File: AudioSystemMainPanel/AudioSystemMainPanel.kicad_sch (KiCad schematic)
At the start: 29 parts, among them J1 AudioPlug3, U1 DEVKIT_V1_ESP32-WROOM-32, U2 PCM5102A, U3 OPA2134, U4 OPA2134

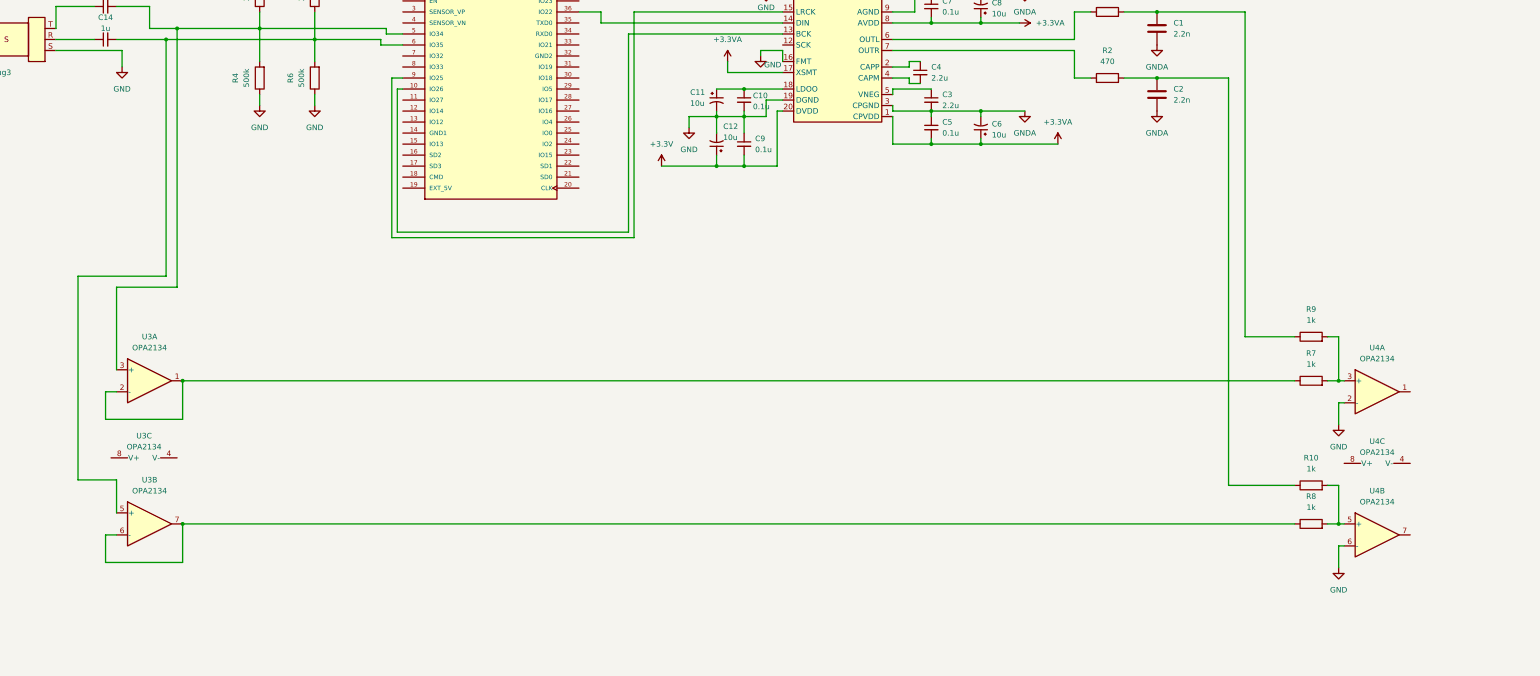
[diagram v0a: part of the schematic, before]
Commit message: added filter/eq panel, small fixes for main panel
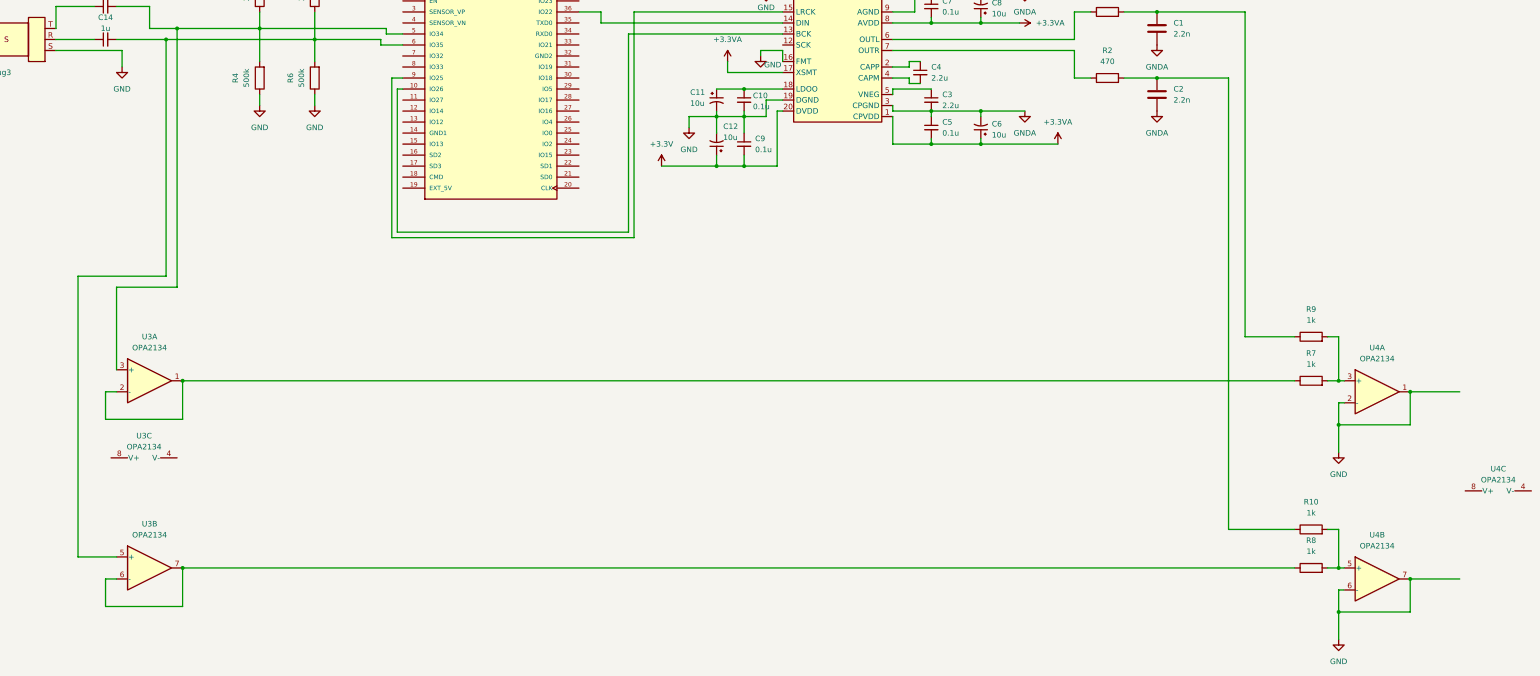
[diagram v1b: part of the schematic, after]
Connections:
- net GND: now also U4.1, U4.7
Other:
- moved on the sheet: R10, R8, U3B, U4B, U4C

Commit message: created noise cancellation panel, added a custom symbol library to project
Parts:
- removed U1: DEVKIT_V1_ESP32-WROOM-32, DEVKIT_V1_ESP32-WROOM-32:MODULE_DEVKIT_V1_ESP32-WROOM-32, symbol DEVKIT_V1_ESP32-WROOM-32:DEVKIT_V1_ESP32-WROOM-32
- added U1: DEVKIT_V1_ESP32-WROOM-32, DEVKIT_V1_ESP32-WROOM-32:MODULE_DEVKIT_V1_ESP32-WROOM-32, symbol AudioSystemSymbolLibrary:DEVKIT_V1_ESP32-WROOM-32
- U3, U4: footprint (none) -> AudioSystemFootprintLibrary:OPA2134UA
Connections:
- net at C14.2, R5.1, R6.2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: now also U1.6 (IO35)
- net at C13.2, R3.1, R4.2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: now also U1.5 (IO34)
- net at U2.13 (BCK): now also U1.10 (IO26)
- net at U2.14 (DIN): now also U1.36 (IO22)
- net at U2.15 (LRCK): now also U1.9 (IO25)
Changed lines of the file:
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@@
 			)
 		)
-		(property "Footprint" ""
+		(property "Footprint" "AudioSystemFootprintLibrary:OPA2134UA"
 			(at 66.04 171.45 0)
 			(effects
@@
 			)
 		)
-		(property "Footprint" ""
+		(property "Footprint" "AudioSystemFootprintLibrary:OPA2134UA"
 			(at 349.25 130.81 0)
 			(effects
@@
 			)
 		)
-		(property "Footprint" ""
+		(property "Footprint" "AudioSystemFootprintLibrary:OPA2134UA"
 			(at 377.19 151.13 0)
 			(effects
@@
 			)
 		)
-		(property "Footprint" ""
+		(property "Footprint" "AudioSystemFootprintLibrary:OPA2134UA"
 			(at 349.25 173.99 0)
 			(effects
@@
 	)
 	(symbol
-		(lib_id "Device:C")
-		(at 298.45 46.99 0)
-		(unit 1)
-		(exclude_from_sim no)
-		(in_bom yes)
-		(on_board yes)
-		(dnp no)
-		(fields_autoplaced yes)
-		(property "Reference" "C1"
-			(at 302.26 45.7199 0)
-			(effects
-				(font
-					(size 1.27 1.27)
-				)
-				(justify left)
-			)
-		)
-		(property "Value" "2.2n"
-			(at 302.26 48.2599 0)
-			(effects
-				(font
-					(size 1.27 1.27)
-				)
-				(justify left)
-			)
-		)
-		(property "Footprint" ""
-			(at 299.4152 50.8 0)
-			(effects
-				(font
-					(size 1.27 1.27)
-				)
-				(hide yes)
-			)
-		)
-		(property "Datasheet" "~"
-			(at 298.45 46.99 0)
-			(effects
-				(font
-					(size 1.27 1.27)
-				)
-				(hide yes)
-			)
-		)
-		(property "Description" "Unpolarized capacitor"
-			(at 298.45 46.99 0)
-			(effects
-				(font
-					(size 1.27 1.27)
-				)
-				(hide yes)
-			)
-		)
-		(pin "1"
-		)
-		(pin "2"
-		)
-		(instances
-			(project ""
-				(path "/ff53e594-6401-4e7d-9332-9d87eb1f5f5d"
-					(reference "C1")
-					(unit 1)
-				)
-			)
-		)
-	)
-	(symbol
-		(lib_id "power:GND")
-		(at 104.14 64.77 0)
-		(unit 1)
-		(exclude_from_sim no)
-		(in_bom yes)
-		(on_board yes)
-		(dnp no)
-		(fields_autoplaced yes)
-		(property "Reference" "#PWR014"
-			(at 104.14 71.12 0)
-			(effects
-				(font
-					(size 1.27 1.27)
-				)
-				(hide yes)
-			)
-		)
-		(property "Value" "GND"
-			(at 104.14 69.85 0)
-			(effects
-				(font
-					(size 1.27 1.27)
-				)
-			)
-		)
-		(property "Footprint" ""
-			(at 104.14 64.77 0)
-			(effects
-				(font
-					(size 1.27 1.27)
-				)
-				(hide yes)
-			)
-		)
-		(property "Datasheet" ""
-			(at 104.14 64.77 0)
-			(effects
-				(font
-					(size 1.27 1.27)
-				)
-				(hide yes)
-			)
-		)
-		(property "Description" "Power symbol creates a global label with name \"GND\" , ground"
-			(at 104.14 64.77 0)
-			(effects
-				(font
-					(size 1.27 1.27)
-				)
-				(hide yes)
-			)
-		)
-		(pin "1"
-		)
-		(instances
-			(project ""
-				(path "/ff53e594-6401-4e7d-9332-9d87eb1f5f5d"
-					(reference "#PWR014")
-					(unit 1)
-				)
-			)
-		)
-	)
-	(symbol
-		(lib_id "DEVKIT_V1_ESP32-WROOM-32:DEVKIT_V1_ESP32-WROOM-32")
+		(lib_id "AudioSystemSymbolLibrary:DEVKIT_V1_ESP32-WROOM-32")
 		(at 144.78 60.96 0)
 		(unit 1)
@@
 			)
 		)
-		(pin "1"
+		(pin "32"
 		)
-		(pin "18"
+		(pin "30"
 		)
-		(pin "2"
+		(pin "6"
 		)
-		(pin "32"
+		(pin "4"
 		)
-		(pin "9"
+		(pin "17"
 		)
-		(pin "27"
+		(pin "12"
 		)
-		(pin "30"
+		(pin "13"
+		)
+		(pin "8"
+		)
+		(pin "33"
+		)
+		(pin "22"
 		)
 		(pin "29"
 		)
-		(pin "15"
+		(pin "34"
 		)
-		(pin "28"
+		(pin "35"
 		)
-		(pin "4"
+		(pin "38"
 		)
-		(pin "24"
+		(pin "9"
 		)
-		(pin "6"
+		(pin "18"
 		)
-		(pin "23"
+		(pin "20"
 		)
-		(pin "12"
+		(pin "25"
 		)
 		(pin "14"
 		)
-		(pin "20"
+		(pin "26"
+		)
+		(pin "37"
 		)
 		(pin "21"
 		)
+		(pin "27"
+		)
+		(pin "28"
+		)
+		(pin "16"
+		)
 		(pin "10"
 		)
-		(pin "3"
+		(pin "2"
 		)
-		(pin "36"
+		(pin "31"
 		)
 		(pin "7"
 		)
-		(pin "22"
+		(pin "15"
+		)
+		(pin "23"
+		)
+		(pin "1"
+		)
+		(pin "3"
+		)
+		(pin "24"
+		)
+		(pin "5"
 		)
 		(pin "11"
@@
 		(pin "19"
 		)
-		(pin "25"
+		(pin "36"
 		)
-		(pin "8"
+		(instances
+			(project ""
+				(path "/ff53e594-6401-4e7d-9332-9d87eb1f5f5d"
+					(reference "U1")
+					(unit 1)
+				)
+			)
 		)
-		(pin "13"
+	)
+	(symbol
+		(lib_id "Device:C")
+		(at 298.45 46.99 0)
+		(unit 1)
+		(exclude_from_sim no)
+		(in_bom yes)
+		(on_board yes)
+		(dnp no)
+		(fields_autoplaced yes)
+		(property "Reference" "C1"
+			(at 302.26 45.7199 0)
+			(effects
+				(font
+					(size 1.27 1.27)
+				)
+				(justify left)
+			)
 		)
-		(pin "16"
+		(property "Value" "2.2n"
+			(at 302.26 48.2599 0)
+			(effects
+				(font
+					(size 1.27 1.27)
+				)
+				(justify left)
+			)
 		)
-		(pin "33"
+		(property "Footprint" ""
+			(at 299.4152 50.8 0)
+			(effects
+				(font
+					(size 1.27 1.27)
+				)
+				(hide yes)
+			)
 		)
-		(pin "37"
+		(property "Datasheet" "~"
+			(at 298.45 46.99 0)
+			(effects
+				(font
+					(size 1.27 1.27)
+				)
+				(hide yes)
+			)
 		)
-		(pin "5"
+		(property "Description" "Unpolarized capacitor"
+			(at 298.45 46.99 0)
+			(effects
+				(font
+					(size 1.27 1.27)
+				)
+				(hide yes)
+			)
 		)
-		(pin "34"
+		(pin "1"
 		)
-		(pin "38"
+		(pin "2"
 		)
-		(pin "26"
+		(instances
+			(project ""
+				(path "/ff53e594-6401-4e7d-9332-9d87eb1f5f5d"
+					(reference "C1")
+					(unit 1)
+				)
+			)
 		)
-		(pin "31"
+	)
+	(symbol
+		(lib_id "power:GND")
+		(at 104.14 64.77 0)
+		(unit 1)
+		(exclude_from_sim no)
+		(in_bom yes)
+		(on_board yes)
+		(dnp no)
+		(fields_autoplaced yes)
+		(property "Reference" "#PWR014"
+			(at 104.14 71.12 0)
+			(effects
+				(font
+					(size 1.27 1.27)
+				)
+				(hide yes)
+			)
 		)
-		(pin "17"
+		(property "Value" "GND"
+			(at 104.14 69.85 0)
+			(effects
+				(font
+					(size 1.27 1.27)
+				)
+			)
 		)
-		(pin "35"
+		(property "Footprint" ""
+			(at 104.14 64.77 0)
+			(effects
+				(font
+					(size 1.27 1.27)
+				)
+				(hide yes)
+			)
+		)
+		(property "Datasheet" ""
+			(at 104.14 64.77 0)
+			(effects
+				(font
+					(size 1.27 1.27)
+				)
+				(hide yes)
+			)
+		)
+		(property "Description" "Power symbol creates a global label with name \"GND\" , ground"
+			(at 104.14 64.77 0)
+			(effects
+				(font
+					(size 1.27 1.27)
+				)
+				(hide yes)
+			)
+		)
+		(pin "1"
 		)
 		(instances
 			(project ""
 				(path "/ff53e594-6401-4e7d-9332-9d87eb1f5f5d"
-					(reference "U1")
+					(reference "#PWR014")
 					(unit 1)
 				)
@@
 			)
 		)
-		(property "Footprint" ""
+		(property "Footprint" "AudioSystemFootprintLibrary:OPA2134UA"
 			(at 64.77 143.51 0)
 			(effects
@@
 			)
 		)
-		(property "Footprint" ""
+		(property "Footprint" "AudioSystemFootprintLibrary:OPA2134UA"
 			(at 66.04 128.27 0)
 			(effects

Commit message: fixed symbol lab problem, added symbols to all ics
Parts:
- U1: footprint DEVKIT_V1_ESP32-WROOM-32:MODULE_DEVKIT_V1_ESP32-WROOM-32 -> AudioSystemFootprintLibrary:MODULE_DEVKIT_V1_ESP32-WROOM-32
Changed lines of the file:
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@@
 			)
 		)
-		(property "Footprint" "DEVKIT_V1_ESP32-WROOM-32:MODULE_DEVKIT_V1_ESP32-WROOM-32"
+		(property "Footprint" "AudioSystemFootprintLibrary:MODULE_DEVKIT_V1_ESP32-WROOM-32"
 			(at 144.78 60.96 0)
 			(effects

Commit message: changed all panels input and output audio interfaces, added noisecancellation panel
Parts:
- removed J1: AudioPlug3, symbol Connector_Audio:AudioPlug3
- added J1, J2: AudioJack3, symbol Connector_Audio:AudioJack3
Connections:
- net GND: now also J1.S, J2.R, J2.S, J2.T
- net at C13.1: now also J1.T
- net at C14.1: now also J1.R
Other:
- moved on the sheet: C1, C10, C11, C12, C13, C14, C2, C3, C4, C5, C6, C7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
